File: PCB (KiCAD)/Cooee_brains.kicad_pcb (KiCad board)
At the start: 2 copper layers, 76.9 x 53.3 mm, 130 parts, among them J1 USB4105-GF-A, J2 Conn_Coaxial_x2_Isolated, J3 Conn_01x07_Socket, SW1 Prog, SW2 Reset, Sw555 ", U1 AMS1117-3.3, U2 ESP32-S3-WROOM-1-N8

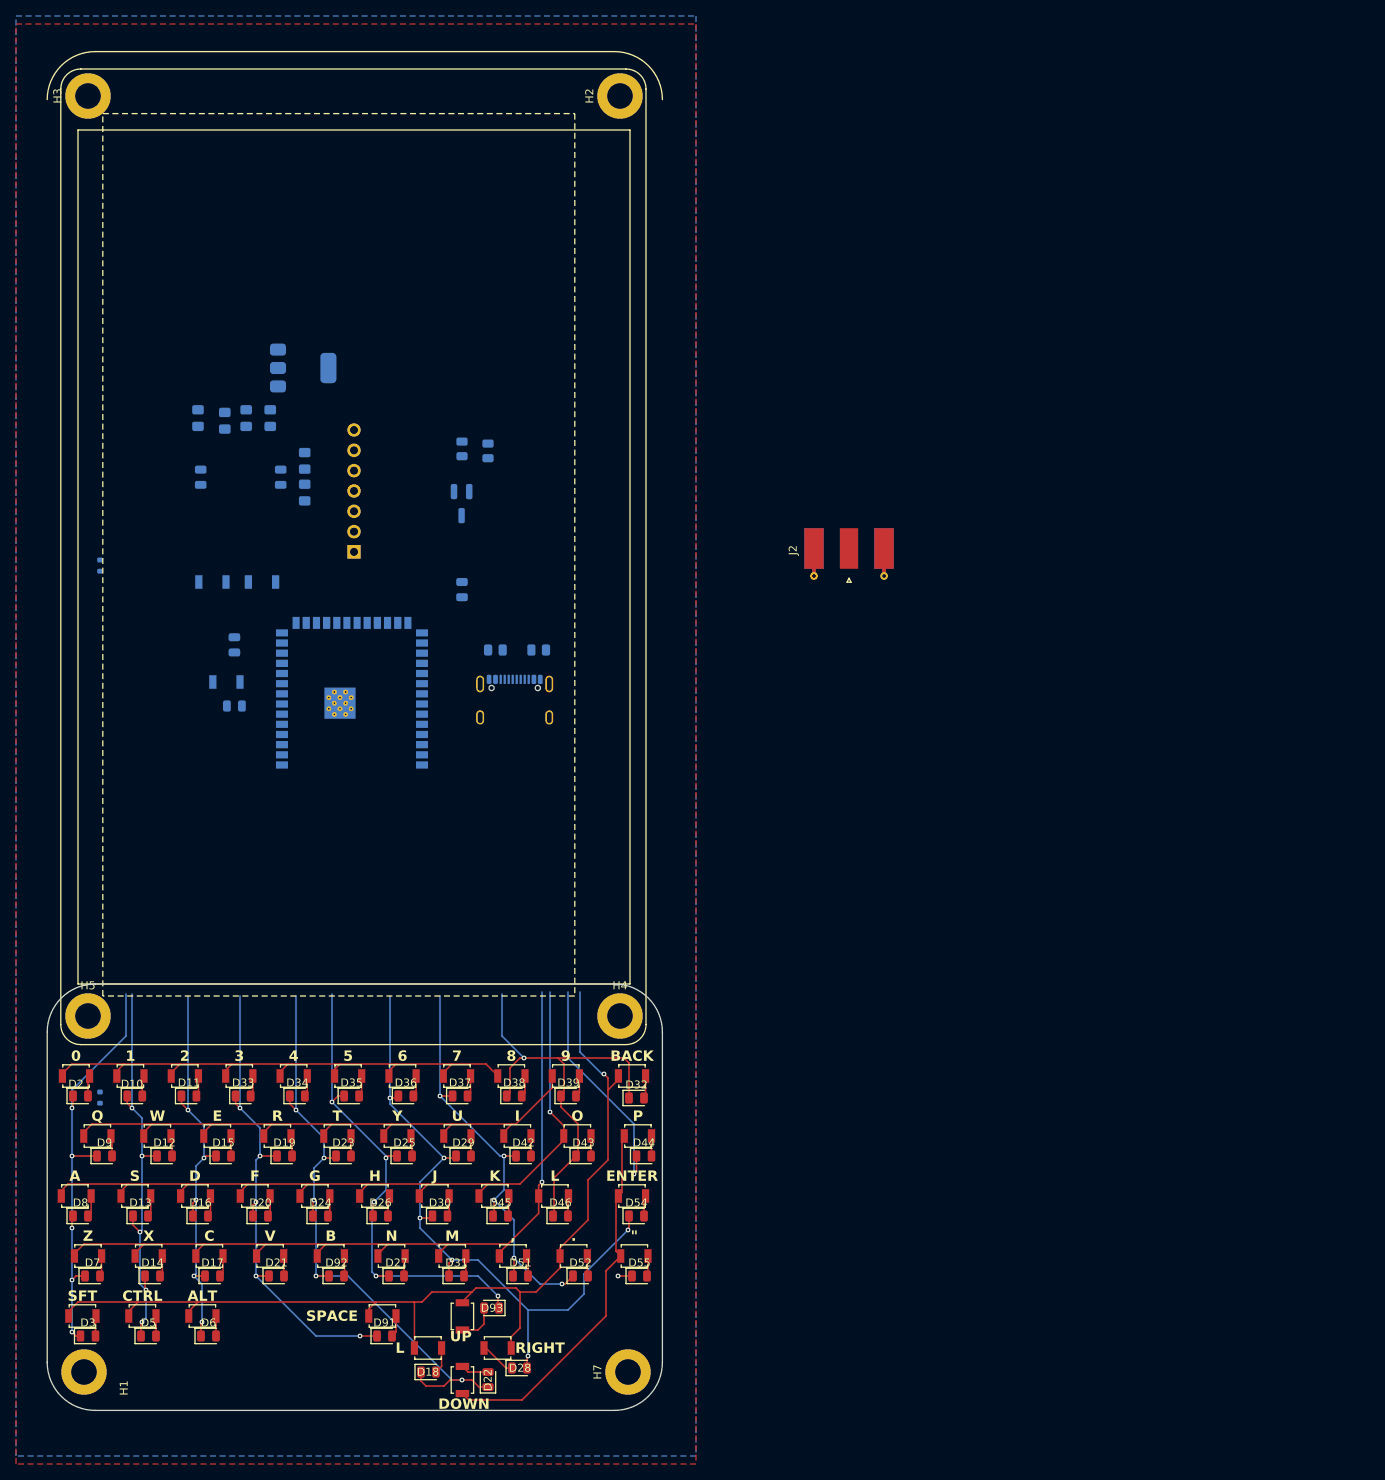
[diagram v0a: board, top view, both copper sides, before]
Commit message: changed computer PCB edge shape to match keyboard
So these can be 2x 2layer boards back to back, easy PnP/hotplate assembly, more modular (replaceable keyboards)
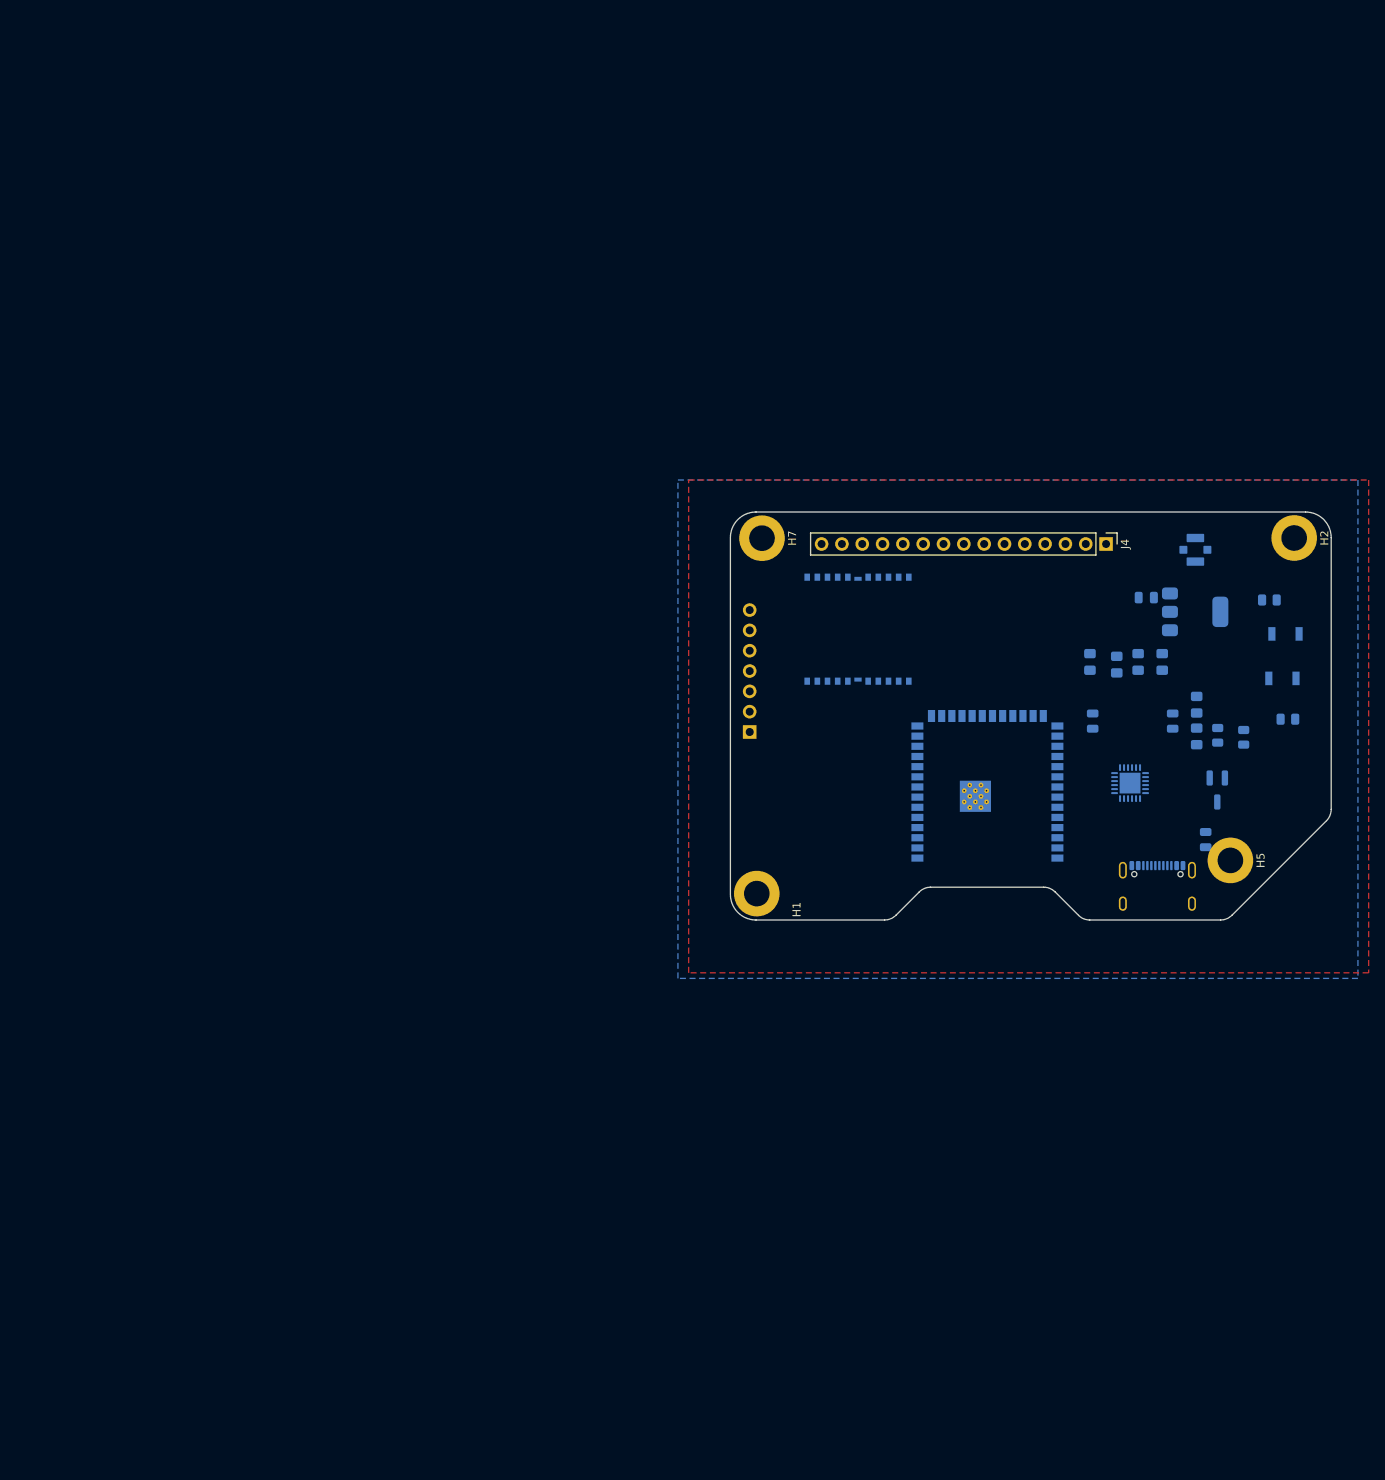
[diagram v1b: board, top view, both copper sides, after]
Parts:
- removed D1, D4: 1N4148WT, Diode_SMD:D_SOD-523
- removed D10, D11, D12, D13, D14, D15, D16, D17, D18, D19, D2, D20, D21, D22, D23, D24, D25, D26, D27, D28, D29, D3, D30, D31, D32, D33, D34, D35, D36, D37, D38, D39, D42, D43, D44, D45, D46, D5, D51, D52, D54, D55, D56, D6, D7, D8, D9, D91, D92, D93: SS24, Diode_SMD:D_0805_2012Metric
- removed ESC1: 0, USB4105-GF-A (1):SW_SPST_B3U-1000P_MovedText
- removed H3, H4: MountingHole, MountingHole:MountingHole_3.2mm_M3_ISO7380_Pad
- removed SWe12: CTRL, USB4105-GF-A (1):SW_SPST_B3U-1000P_MovedText
- removed SWe13, SWe39: L, USB4105-GF-A (1):SW_SPST_B3U-1000P_MovedText
- removed SWe14: U, USB4105-GF-A (1):SW_SPST_B3U-1000P_MovedText
- removed SWe15: J, USB4105-GF-A (1):SW_SPST_B3U-1000P_MovedText
- removed SWe16: M, USB4105-GF-A (1):SW_SPST_B3U-1000P_MovedText
- removed SWe17: BACK, USB4105-GF-A (1):SW_SPST_B3U-1000P_MovedText
- removed SWe18: 2, USB4105-GF-A (1):SW_SPST_B3U-1000P_MovedText
- removed SWe2: DOWN, USB4105-GF-A (1):SW_SPST_B3U-1000P_MovedText
- removed SWe20: 3, USB4105-GF-A (1):SW_SPST_B3U-1000P_MovedText
- removed SWe21: 4, USB4105-GF-A (1):SW_SPST_B3U-1000P_MovedText
- removed SWe24: SFT, USB4105-GF-A (1):SW_SPST_B3U-1000P_MovedText
- removed SWe25: 5, USB4105-GF-A (1):SW_SPST_B3U-1000P_MovedText
- removed SWe26: 6, USB4105-GF-A (1):SW_SPST_B3U-1000P_MovedText
- removed SWe27: 7, USB4105-GF-A (1):SW_SPST_B3U-1000P_MovedText
- removed SWe28: 8, USB4105-GF-A (1):SW_SPST_B3U-1000P_MovedText
- removed SWe29: 9, USB4105-GF-A (1):SW_SPST_B3U-1000P_MovedText
- removed SWe3: ALT, USB4105-GF-A (1):SW_SPST_B3U-1000P_MovedText
- removed SWe32: Q, USB4105-GF-A (1):SW_SPST_B3U-1000P_MovedText
- removed SWe33: A, USB4105-GF-A (1):SW_SPST_B3U-1000P_MovedText
- removed SWe34: Z, USB4105-GF-A (1):SW_SPST_B3U-1000P_MovedText
- removed SWe35: I, USB4105-GF-A (1):SW_SPST_B3U-1000P_MovedText
- removed SWe36: O, USB4105-GF-A (1):SW_SPST_B3U-1000P_MovedText
- removed SWe37: P, USB4105-GF-A (1):SW_SPST_B3U-1000P_MovedText
- removed SWe38: K, USB4105-GF-A (1):SW_SPST_B3U-1000P_MovedText
- removed SWe4: Y, USB4105-GF-A (1):SW_SPST_B3U-1000P_MovedText
- removed SWe42: W, USB4105-GF-A (1):SW_SPST_B3U-1000P_MovedText
- removed SWe43: S, USB4105-GF-A (1):SW_SPST_B3U-1000P_MovedText
- removed SWe44: X, USB4105-GF-A (1):SW_SPST_B3U-1000P_MovedText
- removed SWe47: ,, USB4105-GF-A (1):SW_SPST_B3U-1000P_MovedText
- removed SWe48: ., USB4105-GF-A (1):SW_SPST_B3U-1000P_MovedText
- removed SWe5: H, USB4105-GF-A (1):SW_SPST_B3U-1000P_MovedText
- removed SWe50: ENTER, USB4105-GF-A (1):SW_SPST_B3U-1000P_MovedText
- removed SWe52: E, USB4105-GF-A (1):SW_SPST_B3U-1000P_MovedText
- removed SWe53: D, USB4105-GF-A (1):SW_SPST_B3U-1000P_MovedText
- removed SWe54: C, USB4105-GF-A (1):SW_SPST_B3U-1000P_MovedText
- removed SWe55: POWER, USB4105-GF-A (1):SW_SPST_B3U-1000P_MovedText
- removed SWe6: N, USB4105-GF-A (1):SW_SPST_B3U-1000P_MovedText
- removed SWe62: R, USB4105-GF-A (1):SW_SPST_B3U-1000P_MovedText
- removed SWe63: F, USB4105-GF-A (1):SW_SPST_B3U-1000P_MovedText
- removed SWe64: V, USB4105-GF-A (1):SW_SPST_B3U-1000P_MovedText
- removed SWe7: RIGHT, USB4105-GF-A (1):SW_SPST_B3U-1000P_MovedText
- removed SWe72: T, USB4105-GF-A (1):SW_SPST_B3U-1000P_MovedText
- removed SWe73: G, USB4105-GF-A (1):SW_SPST_B3U-1000P_MovedText
- removed SWe8: 1, USB4105-GF-A (1):SW_SPST_B3U-1000P_MovedText
- removed SWe86: SPACE, USB4105-GF-A (1):SW_SPST_B3U-1000P_MovedText
- removed SWe87: B, USB4105-GF-A (1):SW_SPST_B3U-1000P_MovedText
- removed SWe88: UP, USB4105-GF-A (1):SW_SPST_B3U-1000P_MovedText
- removed Sw555: ", USB4105-GF-A (1):SW_SPST_B3U-1000P_MovedText
- added J4: Conn_01x15_Pin, Connector_PinHeader_2.54mm:PinHeader_1x15_P2.54mm_Vertical, F.Cu at (161.3, 81.0)
- added U3: SX1262IMLTRT, Package_DFN_QFN:QFN-24-1EP_4x4mm_P0.5mm_EP2.6x2.6mm, B.Cu at (164.3, 110.9)
- added U4: RXM-GPS-FM, RF_GPS:Linx_RXM-GPS, B.Cu at (130.2, 91.7)
- J2: footprint Connector_Coaxial:SMA_Molex_73251-1153_EdgeMount_Horizontal -> Connector_Coaxial:U.FL_Molex_MCRF_73412-0110_Vertical; moved to B.Cu
- moved H5 144.1 mm to (176.8, 120.5), turned to -90 degrees
- moved SW2 134.3 mm to (183.7, 92.2)
- moved SW1 128.1 mm to (183.3, 97.8)
- moved C2 115.6 mm to (159.6, 103.1)
- moved C4 115.6 mm to (172.6, 101.1)
- moved D74 115.6 mm to (169.6, 103.1)
- moved R1 115.6 mm to (172.6, 105.0)
- moved R10 115.6 mm to (168.3, 95.7)
- moved R6 115.6 mm to (159.2, 95.7)
- moved R7 115.6 mm to (162.6, 96.1)
- moved R9 115.6 mm to (165.3, 95.7)
- moved U1 115.6 mm to (172.4, 89.5)
- moved C1 114.1 mm to (166.3, 87.7), turned to 0 degrees
- moved H7 105.6 mm to (118.2, 80.3), turned to -90 degrees
- moved H1 103.2 mm to (117.6, 124.7)
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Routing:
- net ROW5: track 127.2 -> 0.00 mm, vias 1 -> 0
- net ROW4: track 102.4 -> 0.00 mm, vias 1 -> 0
- net ROW3: track 98.7 -> 0.00 mm, vias 1 -> 0
- net COL6: track 92.3 -> 0.00 mm, vias 6 -> 0
- net COL7: track 85.1 -> 0.00 mm, vias 6 -> 0
- net COL5: track 78.5 -> 0.00 mm, vias 5 -> 0
- net ROW2: track 76.3 -> 0.00 mm
- net ROW1: track 69.0 -> 0.00 mm
- net COL4: track 61.9 -> 0.00 mm, vias 5 -> 0
- net COL9: track 55.2 -> 0.00 mm, vias 1 -> 0
- net COL8: track 54.5 -> 0.00 mm, vias 5 -> 0
- net COL1: track 54.4 -> 0.00 mm, vias 5 -> 0
- net COL2: track 53.5 -> 0.00 mm, vias 6 -> 0
- net COL3: track 51.5 -> 0.00 mm, vias 5 -> 0
- net ROW6: track 46.8 -> 0.00 mm
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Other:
- board size 76.9 x 53.3 mm -> 75.1 x 51 mm

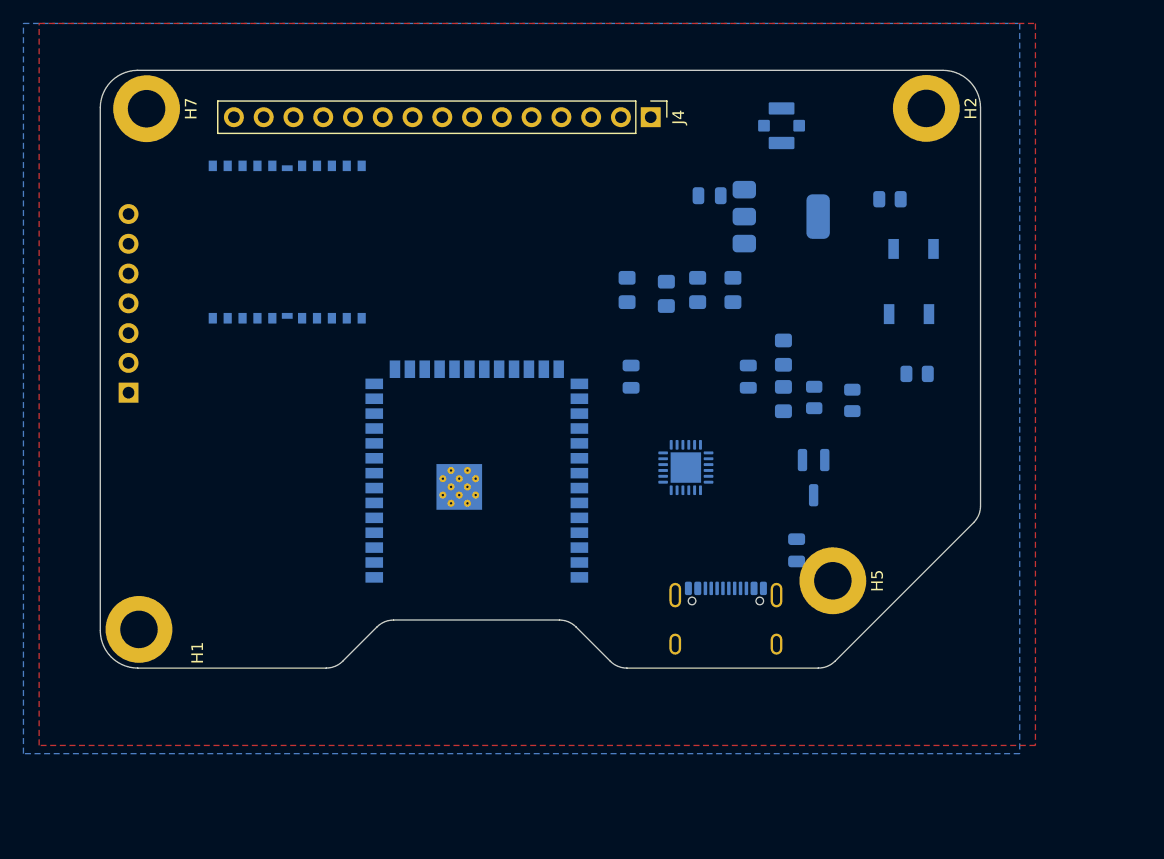
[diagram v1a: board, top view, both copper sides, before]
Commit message: finished keyboard at 67mm
started work on esp32 motherboard
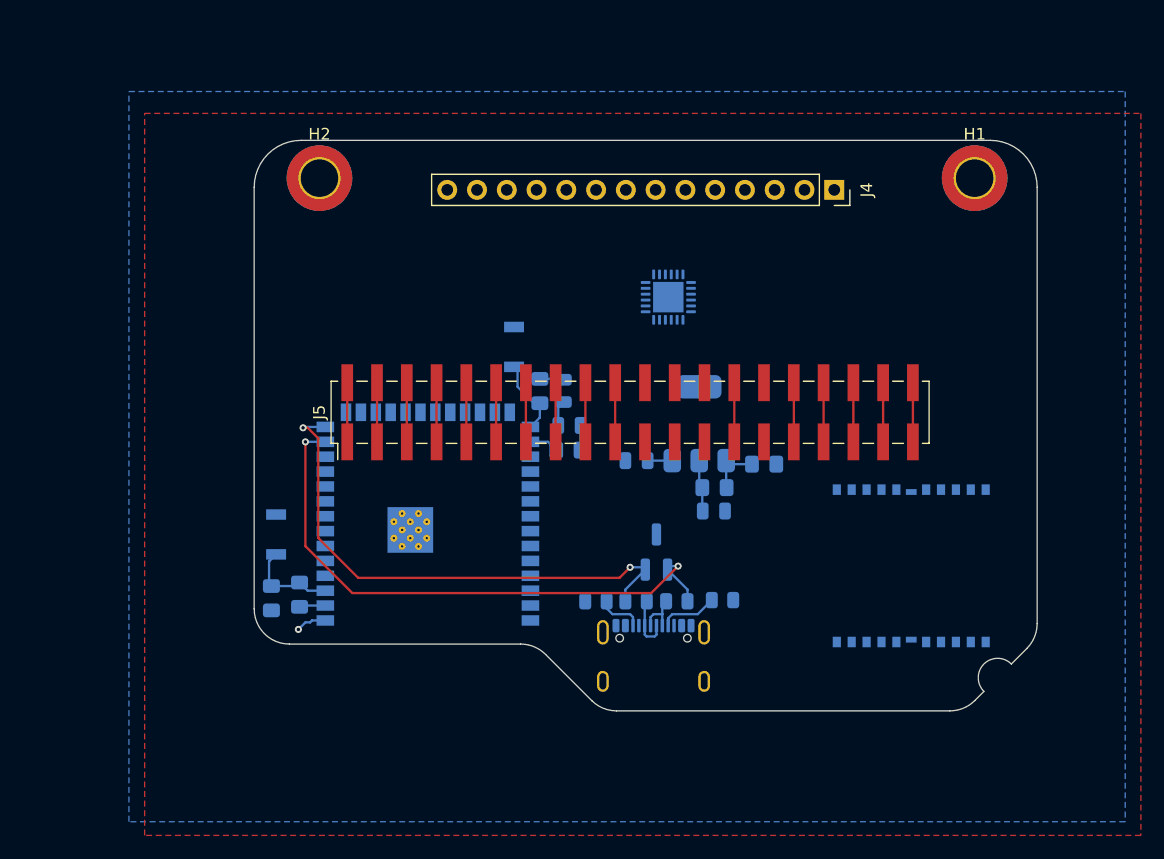
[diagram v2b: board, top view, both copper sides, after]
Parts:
- removed H5, H7: MountingHole, MountingHole:MountingHole_3.2mm_M3_ISO7380_Pad
- removed J2: Conn_Coaxial_x2_Isolated, Connector_Coaxial:U.FL_Molex_MCRF_73412-0110_Vertical
- removed J3: Conn_01x07_Socket, Connector_PinSocket_2.54mm:PinSocket_1x07_P2.54mm_Vertical
- added J5: Conn_02x20_Counter_Clockwise, Connector_PinHeader_2.54mm:PinHeader_2x20_P2.54mm_Vertical_SMD, F.Cu at (159.5, 106.2)
- H1, H2: value MountingHole -> MountingHole_Pad_MP; footprint MountingHole:MountingHole_3.2mm_M3_ISO7380_Pad -> MountingHole:MountingHole_3.2mm_M3_DIN965_Pad_TopBottom
- J4: value Conn_01x15_Pin -> Conn_01x14_Socket; footprint Connector_PinHeader_2.54mm:PinHeader_1x15_P2.54mm_Vertical -> Connector_PinSocket_2.54mm:PinSocket_1x14_P2.54mm_Vertical
- moved H1 81.0 mm to (188.9, 86.2), turned to 0 degrees
- moved U4 60.0 mm to (183.5, 119.3)
- moved SW2 59.6 mm to (129.3, 116.6), turned to 90 degrees
- moved H2 52.1 mm to (133.0, 86.2), turned to 0 degrees
- moved C4 48.4 mm to (128.9, 122.0)
- moved R10 45.2 mm to (131.3, 121.7)
- moved R2 37.1 mm to (167.4, 122.2)
- moved SW1 33.8 mm to (149.6, 100.6), turned to 90 degrees
- moved R3 30.8 mm to (160.0, 122.3)
- moved R5 27.8 mm to (156.6, 122.3), turned to 180 degrees
- moved C3 24.1 mm to (153.8, 104.3), turned to 90 degrees
- moved C1 23.4 mm to (160.1, 110.3)
- moved R4 21.0 mm to (163.5, 122.3), turned to 0 degrees
- moved U1 19.0 mm to (165.4, 107.2), turned to 90 degrees
- moved R1 18.9 mm to (154.2, 109.4), turned to 180 degrees
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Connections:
- J4 pad 1: ROW6 -> unconnected-(J4-Pin_1-Pad1)
- J4 pad 10: COL6 -> OLED_CS
- J4 pad 11: COL5 -> OLED_CLK
- J4 pad 12: COL4 -> OLED_DIN
- J4 pad 13: COL3 -> GND
- J4 pad 14: COL2 -> 3.3V
- J4 pad 2: ROW5 -> unconnected-(J4-Pin_2-Pad2)
- J4 pad 3: ROW4 -> unconnected-(J4-Pin_3-Pad3)
- J4 pad 4: ROW3 -> unconnected-(J4-Pin_4-Pad4)
- J4 pad 5: ROW2 -> unconnected-(J4-Pin_5-Pad5)
- J4 pad 6: ROW1 -> unconnected-(J4-Pin_6-Pad6)
- J4 pad 7: COL9 -> unconnected-(J4-Pin_7-Pad7)
- J4 pad 8: COL8 -> OLED_RST
- J4 pad 9: COL7 -> OLED_DC
- U2 pad 12: COL1 -> unconnected-(U2-IO8-Pad12)
- U2 pad 15: COL6 -> unconnected-(U2-IO3-Pad15)
- U2 pad 17: ROW8 -> unconnected-(U2-IO9-Pad17)
- U2 pad 18: ROW7 -> unconnected-(U2-IO10-Pad18)
- U2 pad 19: ROW6 -> unconnected-(U2-IO11-Pad19)
- U2 pad 20: ROW5 -> unconnected-(U2-IO12-Pad20)
- U2 pad 21: ROW4 -> unconnected-(U2-IO13-Pad21)
- U2 pad 22: ROW3 -> unconnected-(U2-IO14-Pad22)
- U2 pad 38: COL7 -> unconnected-(U2-IO2-Pad38)
- U2 pad 39: COL8 -> unconnected-(U2-IO1-Pad39)
- U2 pad 4: COL5 -> unconnected-(U2-IO4-Pad4)
- U2 pad 5: COL4 -> unconnected-(U2-IO5-Pad5)
- U2 pad 6: COL3 -> unconnected-(U2-IO6-Pad6)
- U2 pad 7: COL2 -> unconnected-(U2-IO7-Pad7)
- U2 pad 8: ROW2 -> unconnected-(U2-IO15-Pad8)
- U2 pad 9: ROW1 -> unconnected-(U2-IO16-Pad9)
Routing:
- net USB_DN: track 0.00 -> 49.4 mm, vias 0 -> 2
- net USB_DP: track 0.00 -> 45.3 mm, vias 0 -> 2
- net 3.3V: track 0.00 -> 8.65 mm
- net EN: track 0.00 -> 8.04 mm
- net IO0: track 0.00 -> 6.66 mm
- net ROW2: track 0.00 -> 5.05 mm
- net COL7: track 0.00 -> 5.05 mm
- net COL4: track 0.00 -> 5.05 mm
- net ROW5: track 0.00 -> 5.05 mm
- net ROW4: track 0.00 -> 5.05 mm
- net ROW3: track 0.00 -> 5.05 mm
- net ROW1: track 0.00 -> 5.05 mm
- net COL9: track 0.00 -> 5.05 mm
- net COL8: track 0.00 -> 5.05 mm
- net COL6: track 0.00 -> 5.05 mm
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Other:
- board size 75.1 x 51 mm -> 66.8 x 48.7 mm
